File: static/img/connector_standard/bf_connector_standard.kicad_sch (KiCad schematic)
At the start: 9 parts, among them J1 ESC Connector, J2 Extended ESC Connector, J3 UART Connector, J4 UART + I2C Connector, J5 I2C Connector, J6 Camera Connector, J7 Analog VTX Connector, J8 Digital VTX Connector, J9 SWD Connector

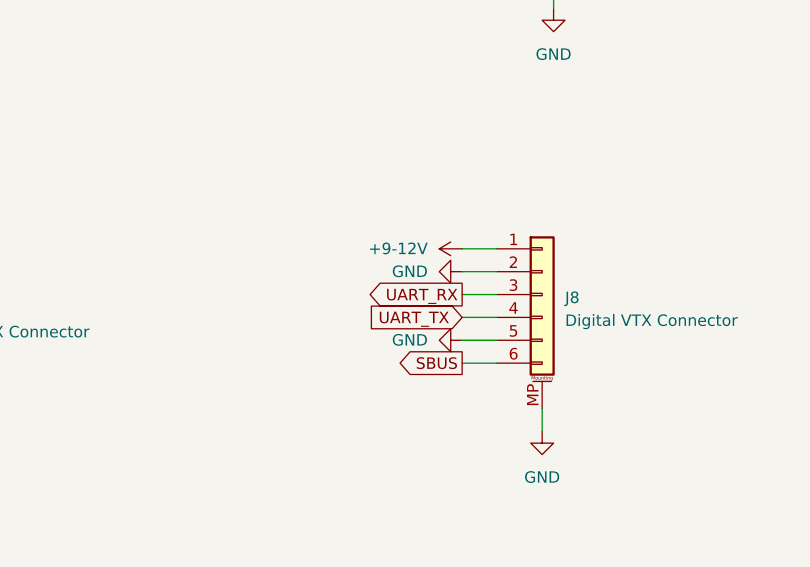
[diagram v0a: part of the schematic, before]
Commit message: Content: Fix Digital VTX Connector
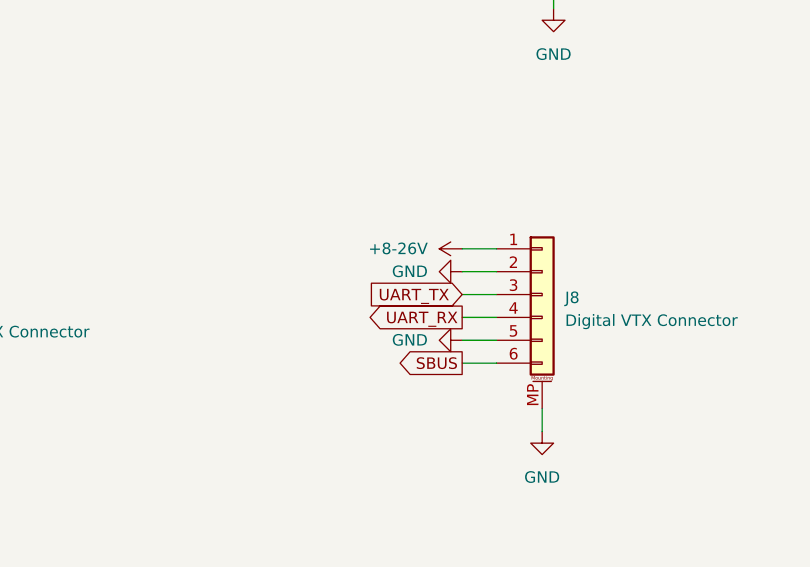
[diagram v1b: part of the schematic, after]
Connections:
- net +9-12V: no longer J8.1 (Pin_1)
- net UART_RX: now also J8.4 (Pin_4); no longer J8.3 (Pin_3)
- net UART_TX: now also J8.3 (Pin_3); no longer J8.4 (Pin_4)
- new net +8-26V: J8.1 (Pin_1)
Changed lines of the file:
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@@
 	(global_label "UART_TX"
 		(shape input)
-		(at 227.33 101.6 180)
-		(fields_autoplaced yes)
-		(effects
-			(font
-				(size 1.27 1.27)
-			)
-			(justify right)
-		)
-		(property "Intersheetrefs" "${INTERSHEET_REFS}"
-			(at 216.9155 101.6 0)
+		(at 227.33 99.06 180)
+		(fields_autoplaced yes)
+		(effects
+			(font
+				(size 1.27 1.27)
+			)
+			(justify right)
+		)
+		(property "Intersheetrefs" "${INTERSHEET_REFS}"
+			(at 216.9155 99.06 0)
 			(effects
 				(font
@@
 	(global_label "UART_RX"
 		(shape output)
-		(at 227.33 99.06 180)
-		(fields_autoplaced yes)
-		(effects
-			(font
-				(size 1.27 1.27)
-			)
-			(justify right)
-		)
-		(property "Intersheetrefs" "${INTERSHEET_REFS}"
-			(at 216.9155 99.06 0)
+		(at 227.33 101.6 180)
+		(fields_autoplaced yes)
+		(effects
+			(font
+				(size 1.27 1.27)
+			)
+			(justify right)
+		)
+		(property "Intersheetrefs" "${INTERSHEET_REFS}"
+			(at 216.9155 101.6 0)
 			(effects
 				(font
@@
 			)
 		)
-		(property "Value" "+9-12V"
+		(property "Value" "+8-26V"
 			(at 223.52 93.9799 90)
 			(effects

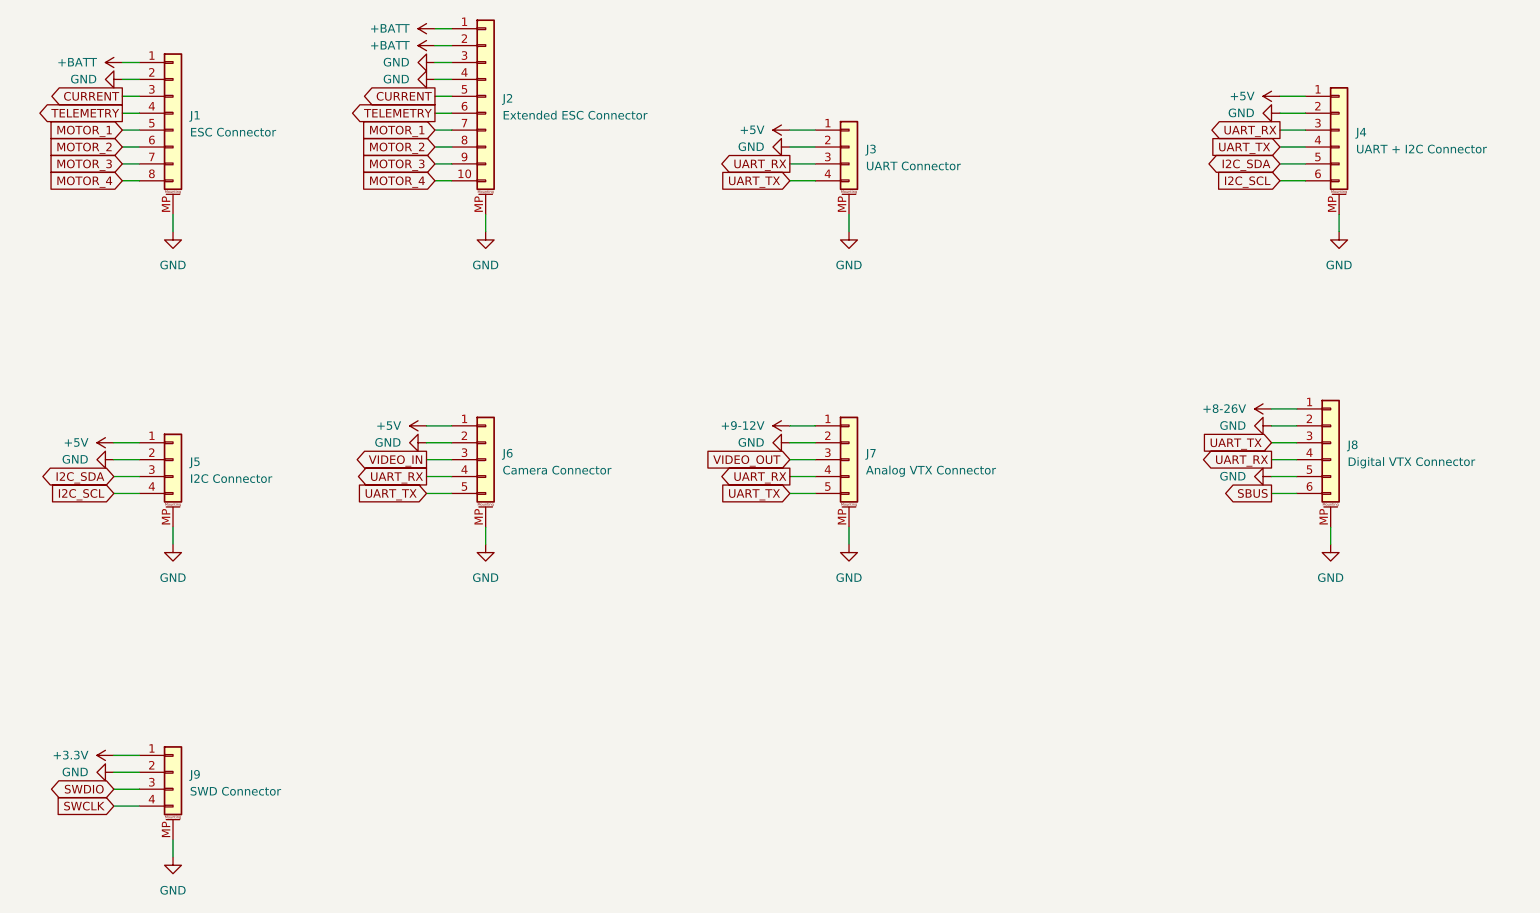
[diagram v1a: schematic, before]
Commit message: Content: Add 3 and 4-pin camera connectors (#610)
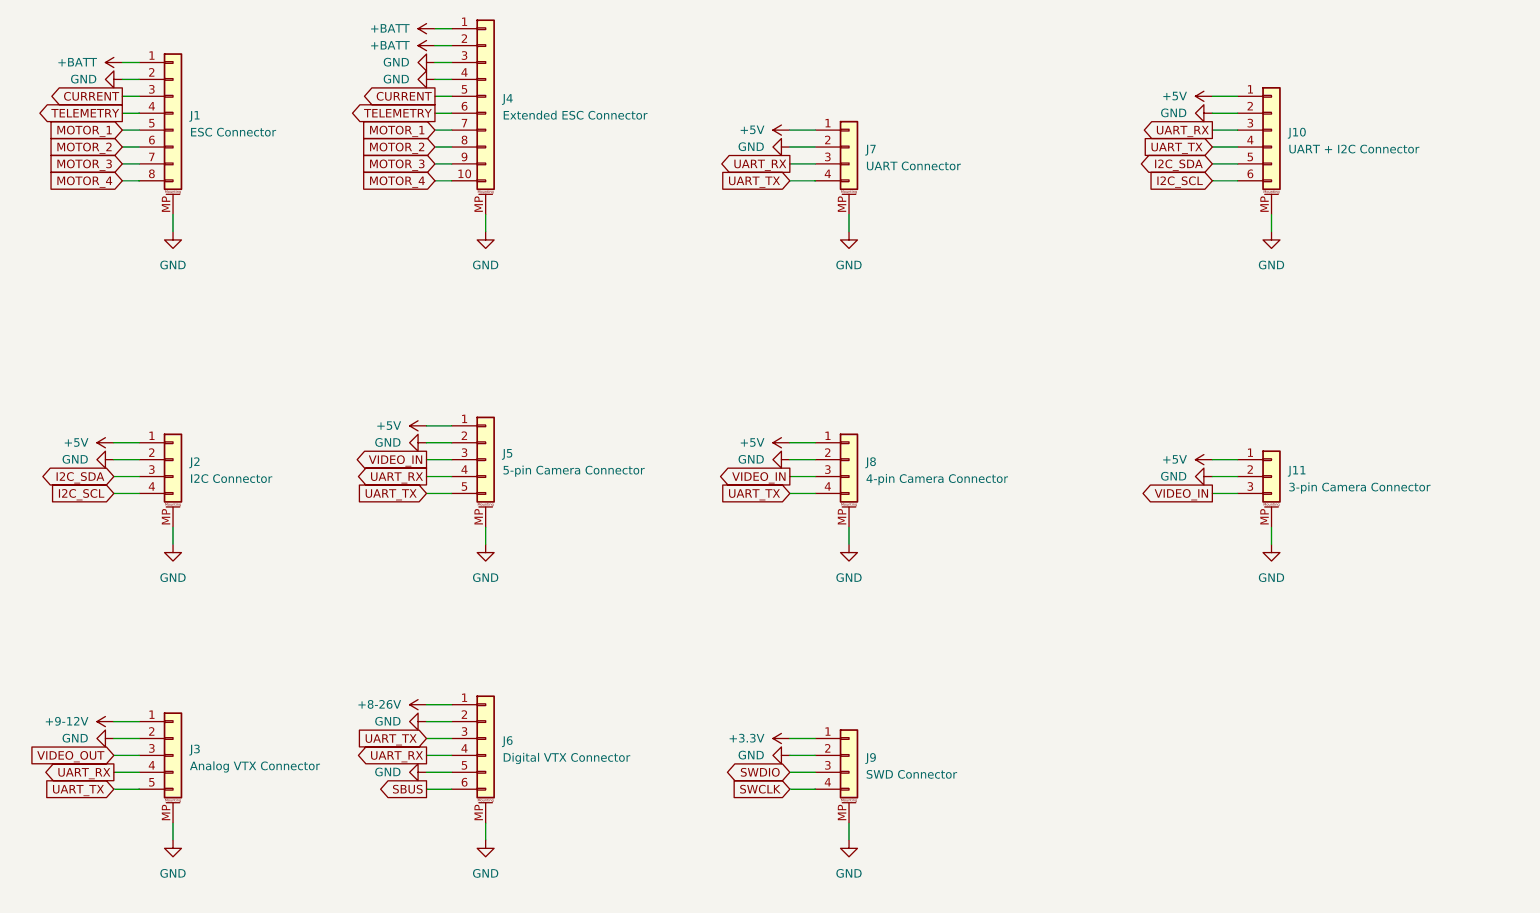
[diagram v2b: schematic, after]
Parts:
- added J11: 3-pin Camera Connector, Connector_JST:JST_SH_SM03B-SRSS-TB_1x03-1MP_P1.00mm_Horizontal, symbol Connector_Generic_MountingPin:Conn_01x03_MountingPin
- added J8: 4-pin Camera Connector, Connector_JST:JST_SH_SM04B-SRSS-TB_1x04-1MP_P1.00mm_Horizontal, symbol Connector_Generic_MountingPin:Conn_01x04_MountingPin
- J5: renamed from J6; value Camera Connector -> 5-pin Camera Connector
- renumbered J4 to J10, J5 to J2, J7 to J3, J2 to J4, J8 to J6, J3 to J7
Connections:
- net +5V: now also J11.1 (Pin_1), J8.1 (Pin_1)
- net GND: now also J11.2 (Pin_2), J11.MP (MountPin), J8.2 (Pin_2), J8.MP (MountPin)
- net UART_TX: now also J8.4 (Pin_4)
- net VIDEO_IN: now also J11.3 (Pin_3), J8.3 (Pin_3)
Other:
- moved on the sheet: J10, J3, J6, J9
